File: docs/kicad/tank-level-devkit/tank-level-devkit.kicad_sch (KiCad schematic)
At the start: 16 parts, among them J1 JSN-SR04T, J2 Panel_USB-A_F, Q1 AO3401A, Q2 2N3904, U1 ESP32_DevKit_V1, U2 MT3608, U3 TP4056

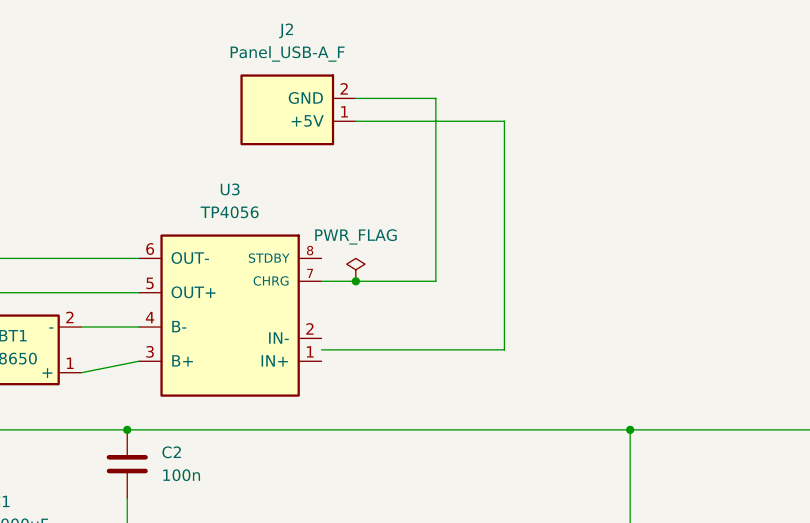
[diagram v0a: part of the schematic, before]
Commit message: Update tank-level KiCad schematic wiring for CHRG and pull-up.
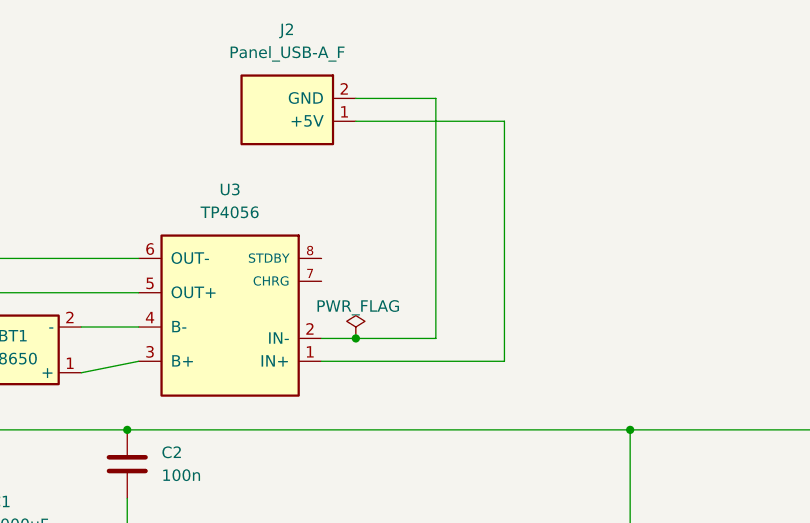
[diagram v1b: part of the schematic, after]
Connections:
- net at J2.1 (+5V): now also U3.1 (IN+)
- net at J2.2 (GND): now also U3.2 (IN-); no longer U3.7 (CHRG)
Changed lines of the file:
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@@
 	)
 	(junction
-		(at 195.58 87.63)
+		(at 195.58 93.98)
 		(diameter 0)
 		(color 0 0 0 1)
@@
 	(wire
 		(pts
-			(xy 212.09 95.25) (xy 191.77 95.25)
+			(xy 212.09 96.52) (xy 191.77 96.52)
 		)
 		(stroke
@@
 	(wire
 		(pts
-			(xy 204.47 87.63) (xy 195.58 87.63)
+			(xy 204.47 93.98) (xy 195.58 93.98)
 		)
 		(stroke
@@
 	(wire
 		(pts
-			(xy 212.09 69.85) (xy 212.09 95.25)
-		)
-		(stroke
-			(width 0)
-			(type default)
-			(color 194 0 0 1)
-		)
-	)
-	(wire
-		(pts
-			(xy 204.47 67.31) (xy 204.47 87.63)
+			(xy 212.09 69.85) (xy 212.09 96.52)
+		)
+		(stroke
+			(width 0)
+			(type default)
+			(color 194 0 0 1)
+		)
+	)
+	(wire
+		(pts
+			(xy 204.47 67.31) (xy 204.47 93.98)
 		)
 		(stroke
@@
 	(wire
 		(pts
-			(xy 195.58 87.63) (xy 191.77 87.63)
+			(xy 195.58 93.98) (xy 191.77 93.98)
 		)
 		(stroke
@@
 		(lib_name "PWR_FLAG_4")
 		(lib_id "power:PWR_FLAG")
-		(at 195.58 87.63 0)
+		(at 195.58 93.98 0)
 		(unit 1)
 		(body_style 1)
@@
 		(in_pos_files yes)
 		(dnp no)
-		(fields_autoplaced yes)
 		(property "Reference" "#FLG02"
-			(at 195.58 85.725 0)
+			(at 195.58 92.075 0)
 			(hide yes)
 			(show_name no)
@@
 		)
 		(property "Value" "PWR_FLAG"
-			(at 195.58 82.55 0)
+			(at 195.834 90.424 0)
 			(show_name no)
 			(do_not_autoplace no)
@@
 		)
 		(property "Footprint" ""
-			(at 195.58 87.63 0)
+			(at 195.58 93.98 0)
 			(hide yes)
 			(show_name no)
@@
 		)
 		(property "Datasheet" ""
-			(at 195.58 87.63 0)
+			(at 195.58 93.98 0)
 			(hide yes)
 			(show_name no)
@@
 		)
 		(property "Description" "Special symbol for telling ERC where power comes from"
-			(at 195.58 87.63 0)
-			(hide yes)
-			(show_name no)
+			(at 195.58 93.98 0)
+			(hide yes)
+			(show_name no)
